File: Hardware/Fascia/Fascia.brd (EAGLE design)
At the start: 108.5 x 29.5 mm, 0 parts

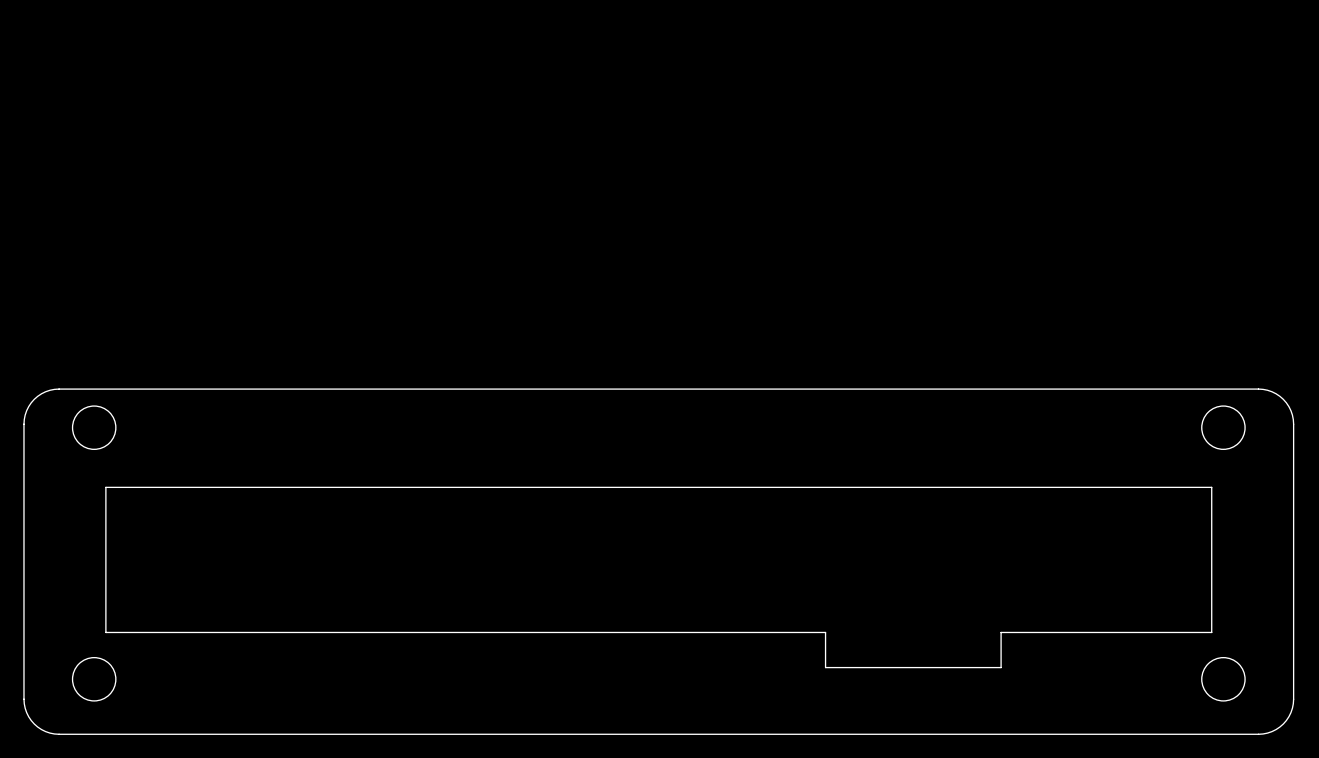
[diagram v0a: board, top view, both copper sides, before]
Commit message: Tiled Fascia's for laser cutter
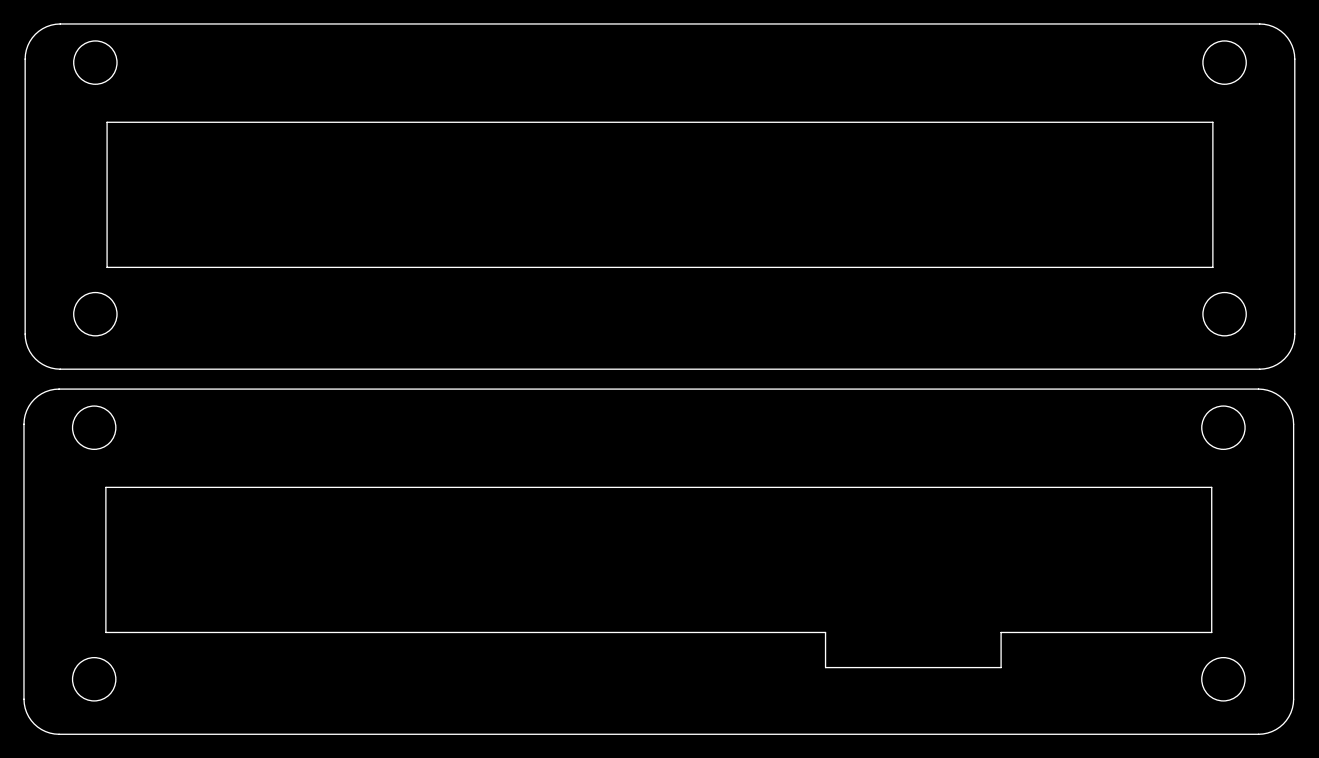
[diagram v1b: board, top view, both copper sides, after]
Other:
- board size 108.5 x 29.5 mm -> 108.6 x 60.7 mm
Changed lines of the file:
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@@
 <wire x1="68.5" y1="8.7" x2="7" y2="8.7" width="0.1" layer="20"/>
 <wire x1="7" y1="8.7" x2="7" y2="21.1" width="0.1" layer="20"/>
+<wire x1="0.1" y1="34.2" x2="3.1" y2="31.2" width="0.1" layer="20" curve="90"/>
+<wire x1="3.1" y1="31.2" x2="105.6" y2="31.2" width="0.1" layer="20"/>
+<wire x1="105.6" y1="31.2" x2="108.6" y2="34.2" width="0.1" layer="20" curve="90"/>
+<wire x1="108.6" y1="34.2" x2="108.6" y2="57.7" width="0.1" layer="20"/>
+<wire x1="108.6" y1="57.7" x2="105.6" y2="60.7" width="0.1" layer="20" curve="90"/>
+<wire x1="105.6" y1="60.7" x2="3.1" y2="60.7" width="0.1" layer="20"/>
+<wire x1="3.1" y1="60.7" x2="0.1" y2="57.7" width="0.1" layer="20" curve="90"/>
+<wire x1="0.1" y1="57.7" x2="0.1" y2="34.2" width="0.1" layer="20"/>
+<hole x="6.1" y="57.4" drill="3.7"/>
+<hole x="102.6" y="57.4" drill="3.7"/>
+<hole x="6.1" y="35.9" drill="3.7"/>
+<hole x="102.6" y="35.9" drill="3.7"/>
+<wire x1="7.1" y1="52.3" x2="101.6" y2="52.3" width="0.1" layer="20"/>
+<wire x1="101.6" y1="52.3" x2="101.6" y2="39.9" width="0.1" layer="20"/>
+<wire x1="101.6" y1="39.9" x2="7.1" y2="39.9" width="0.1" layer="20"/>
+<wire x1="7.1" y1="39.9" x2="7.1" y2="52.3" width="0.1" layer="20"/>
 </plain>
 <attributes>
